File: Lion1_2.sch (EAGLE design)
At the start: 74 parts, among them IC1 MCP4822, IC2 MCP4822, IC3 MCP4822, IC4 REG1117, U7 2564-, U8 2564-

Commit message: v2
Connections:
- net N$24 renamed TX2
- net N$85 renamed RX2
- removed net 3V3: JP1.4, JP10.2, JP10.4, JP10.6
- net 3V3_7: now also JP15.1
- net 3V3_8: now also JP1.4, JP10.2, JP10.4, JP10.6
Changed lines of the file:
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@@
-</segment>
-</net>
-<net name="3V3" class="0">
-<segment>
-<pinref part="JP1" gate="A" pin="4"/>
-<wire x1="177.165" y1="55.245" x2="167.64" y2="55.245" width="0.1524" layer="91"/>
-<label x="167.64" y="55.245" size="1.778" layer="95"/>
-</segment>
-<segment>
-<wire x1="194.945" y1="38.1" x2="184.785" y2="38.1" width="0.1524" layer="91"/>
-<label x="191.135" y="38.1" size="1.778" layer="95"/>
-<pinref part="JP10" gate="A" pin="6"/>
-</segment>
-<segment>
-<wire x1="194.31" y1="43.18" x2="184.785" y2="43.18" width="0.1524" layer="91"/>
-<label x="191.135" y="43.18" size="1.778" layer="95"/>
-<pinref part="JP10" gate="A" pin="2"/>
-</segment>
-<segment>
-<wire x1="194.31" y1="40.64" x2="184.785" y2="40.64" width="0.1524" layer="91"/>
-<label x="191.135" y="40.64" size="1.778" layer="95"/>
-<pinref part="JP10" gate="A" pin="4"/>
 </segment>
 </net>
@@
 </segment>
 </net>
-<net name="N$85" class="0">
+<net name="RX2" class="0">
 <segment>
 <pinref part="U7" gate="-36" pin="KL"/>
 <pinref part="JP15" gate="A" pin="3"/>
 <wire x1="133.985" y1="59.69" x2="151.765" y2="59.69" width="0.1524" layer="91"/>
+<label x="133.985" y="59.69" size="1.778" layer="95"/>
 </segment>
 </net>
@@
 </segment>
 </net>
-<net name="N$24" class="0">
+<net name="TX2" class="0">
 <segment>
 <wire x1="103.505" y1="59.69" x2="116.84" y2="59.69" width="0.1524" layer="91"/>
@@
 <pinref part="JP15" gate="A" pin="2"/>
 <pinref part="U7" gate="-35" pin="KL"/>
+<label x="102.87" y="59.69" size="1.778" layer="95"/>
 </segment>
 </net>
@@
 <label x="-27.94" y="111.125" size="1.778" layer="95"/>
 </segment>
+<segment>
+<wire x1="194.31" y1="43.18" x2="184.785" y2="43.18" width="0.1524" layer="91"/>
+<label x="191.135" y="43.18" size="1.778" layer="95"/>
+<pinref part="JP10" gate="A" pin="2"/>
+</segment>
+<segment>
+<wire x1="194.31" y1="40.64" x2="184.785" y2="40.64" width="0.1524" layer="91"/>
+<label x="191.135" y="40.64" size="1.778" layer="95"/>
+<pinref part="JP10" gate="A" pin="4"/>
+</segment>
+<segment>
+<wire x1="194.945" y1="38.1" x2="184.785" y2="38.1" width="0.1524" layer="91"/>
+<label x="191.135" y="38.1" size="1.778" layer="95"/>
+<pinref part="JP10" gate="A" pin="6"/>
+</segment>
+<segment>
+<pinref part="JP1" gate="A" pin="4"/>
+<wire x1="177.165" y1="55.245" x2="167.64" y2="55.245" width="0.1524" layer="91"/>
+<label x="167.64" y="55.245" size="1.778" layer="95"/>
+</segment>
 </net>
 <net name="3V3_7" class="0">
@@
 <segment>
 <pinref part="U7" gate="-4" pin="KL"/>
-<wire x1="133.985" y1="100.33" x2="136.525" y2="100.33" width="0.1524" layer="91"/>
 <label x="133.985" y="100.33" size="1.778" layer="95"/>
-</segment>
-<segment>
+<pinref part="JP15" gate="A" pin="1"/>
+<wire x1="133.985" y1="100.33" x2="151.765" y2="100.33" width="0.1524" layer="91"/>
+<wire x1="151.765" y1="100.33" x2="151.765" y2="64.77" width="0.1524" layer="91"/>
+</segment>
+<segment>

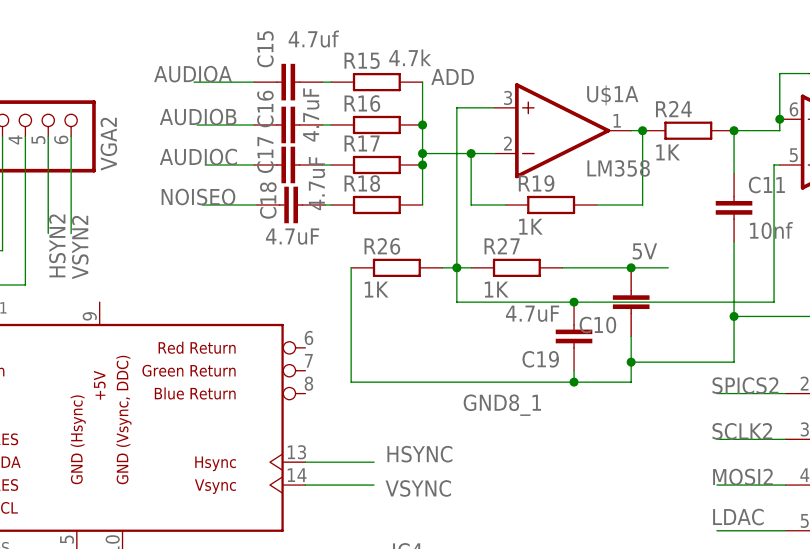
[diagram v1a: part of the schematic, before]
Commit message: some syslib functions, audio sample play command, 1 resistor added
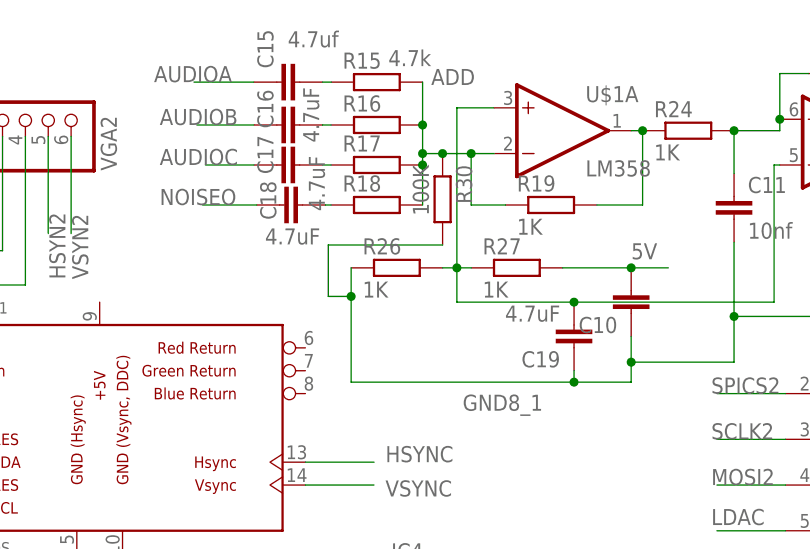
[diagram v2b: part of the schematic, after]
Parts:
- added R30: 100K, SmartPrj:R-EU_0204/7
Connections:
- net ADD: now also R30.1
- net GND8_1: now also R30.2
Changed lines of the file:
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@@
 <setting verticaltext="up"/>
 </settings>
-<grid distance="0.0125" unitdist="inch" unit="inch" style="lines" multiple="1" display="no" altdistance="0.01" altunitdist="inch" altunit="inch"/>
+<grid distance="0.025" unitdist="inch" unit="inch" style="lines" multiple="1" display="no" altdistance="0.01" altunitdist="inch" altunit="inch"/>
 <layers>
 <layer number="1" name="Top" color="4" fill="1" visible="no" active="no"/>
@@
 <part name="C22" library="rcl" deviceset="C-EU" device="050-025X075" value="4.7uf"/>
 <part name="R29" library="SmartPrj" deviceset="R-EU_" device="0204/2V"/>
+<part name="R30" library="SmartPrj" deviceset="R-EU_" device="0204/7" value="100K"/>
 </parts>
 <sheets>
@@
 </instance>
 <instance part="R29" gate="G$1" x="185.1025" y="127"/>
+<instance part="R30" gate="G$1" x="132.08" y="171.45" rot="R270"/>
 </instances>
 <busses>
@@
 <wire x1="137.795" y1="176.53" x2="135.255" y2="176.53" width="0.1524" layer="91"/>
 <pinref part="R19" gate="G$1" pin="1"/>
-<wire x1="135.255" y1="176.53" x2="129.8575" y2="176.53" width="0.1524" layer="91"/>
+<wire x1="135.255" y1="176.53" x2="132.08" y2="176.53" width="0.1524" layer="91"/>
+<wire x1="132.08" y1="176.53" x2="129.8575" y2="176.53" width="0.1524" layer="91"/>
 <wire x1="139.065" y1="170.815" x2="135.255" y2="170.815" width="0.1524" layer="91"/>
 <wire x1="135.255" y1="170.815" x2="135.255" y2="176.53" width="0.1524" layer="91"/>
@@
 <junction x="129.8575" y="175.26"/>
 <label x="130.81" y="184.15" size="1.778" layer="95"/>
+<pinref part="R30" gate="G$1" pin="1"/>
+<junction x="132.08" y="176.53"/>
 </segment>
 <segment>
@@
 <pinref part="R26" gate="G$1" pin="1"/>
 <wire x1="146.685" y1="151.13" x2="121.92" y2="151.13" width="0.1524" layer="91"/>
-<wire x1="121.92" y1="151.13" x2="121.92" y2="163.83" width="0.1524" layer="91"/>
+<wire x1="121.92" y1="151.13" x2="121.92" y2="160.655" width="0.1524" layer="91"/>
 <pinref part="C11" gate="G$1" pin="2"/>
+<wire x1="121.92" y1="160.655" x2="121.92" y2="163.83" width="0.1524" layer="91"/>
 <wire x1="164.465" y1="166.6875" x2="164.465" y2="158.4325" width="0.1524" layer="91"/>
 <wire x1="164.465" y1="158.4325" x2="164.465" y2="153.3525" width="0.1524" layer="91"/>
@@
 <pinref part="U$1" gate="P" pin="V-"/>
 <junction x="191.77" y="158.4325"/>
-</segment>
-<segment>
+<pinref part="R30" gate="G$1" pin="2"/>
+<wire x1="132.08" y1="166.37" x2="119.38" y2="166.37" width="0.1524" layer="91"/>
+<wire x1="119.38" y1="166.37" x2="119.38" y2="160.655" width="0.1524" layer="91"/>
+<wire x1="119.38" y1="160.655" x2="121.92" y2="160.655" width="0.1524" layer="91"/>
+<junction x="121.92" y="160.655"/>
+</segment>
+<segment>
